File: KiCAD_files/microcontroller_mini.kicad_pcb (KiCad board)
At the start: 4 copper layers, 21 x 51 mm, 38 parts, among them J1 Conn_02x20_Top_Bottom, J2 USB_B_Micro, J8 Conn_02x07_Odd_Even, SW1 SW_Push, U1 STM32G474RE, U2 AT25xxx, U3 WE-TVS-82400102, U4 AP1117-33, Y1 ECS-240-10-33-AGM-TR - 24MHz

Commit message: [Feeder] WIP on the V2 redesign
Former-commit-id: 5bce92fb9a428cd005e74b891f189b6460f88472
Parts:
- R1: value 1 -> 1R

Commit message: WIP : 99 percents of the nets are now routed properly
Former-commit-id: fcbb95e3f0a6512a63faba729c3990d7109d7768
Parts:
- moved J2 0.81 mm to (95.6, 51.2)
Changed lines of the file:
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@@
   )
   (footprint "Connector_USB:USB_Micro-B_Molex_47346-0001" (layer "F.Cu")
-    (at 95.560978 52.01 180)
+    (at 95.560978 51.2 180)
     (descr "Micro USB B receptable with flange, bottom-mount, SMD, right-angle (http://www.molex.com/pdm_docs/sd/473460001_sd.pdf)")
     (tags "Micro B USB SMD")

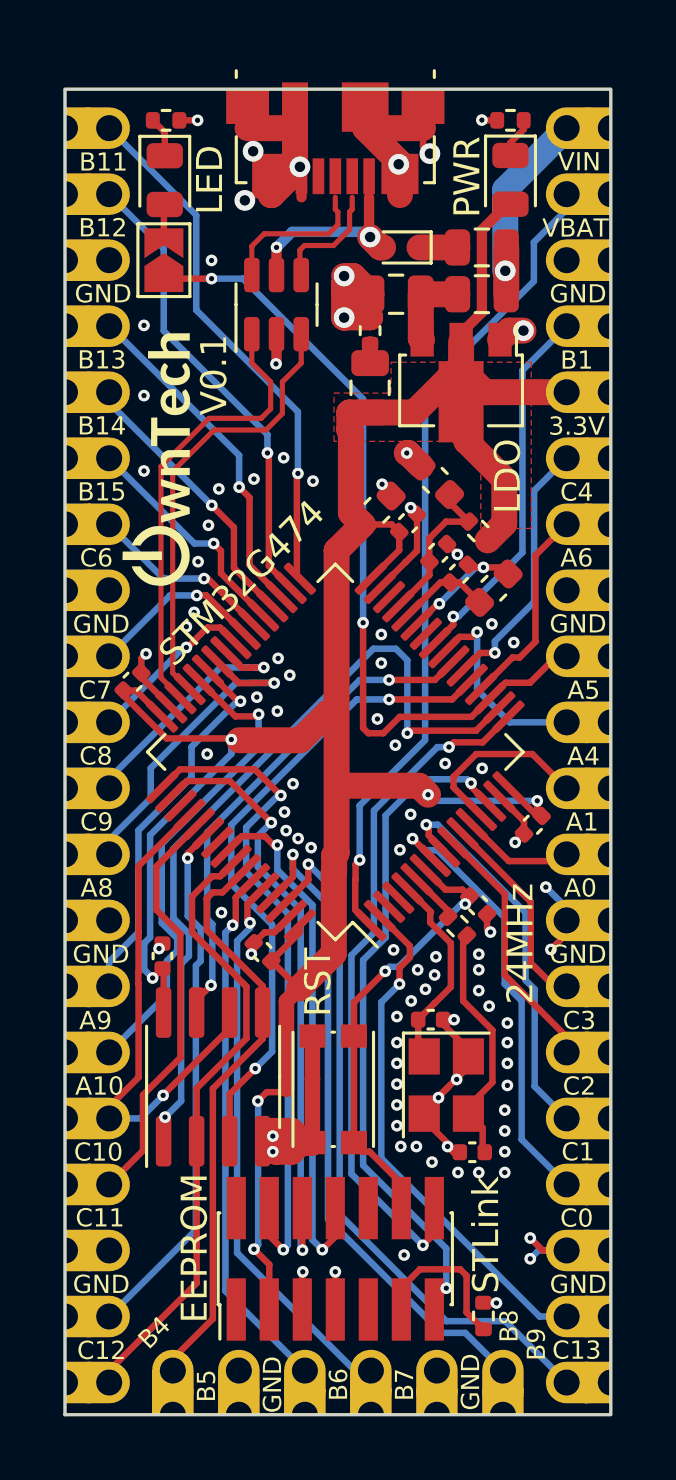
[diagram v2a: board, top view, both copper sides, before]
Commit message: WIP : Started correcting MCU board mistakes
Former-commit-id: 0e34b6d72e10d1eac13c8cf31fc8e8f14d7f468b
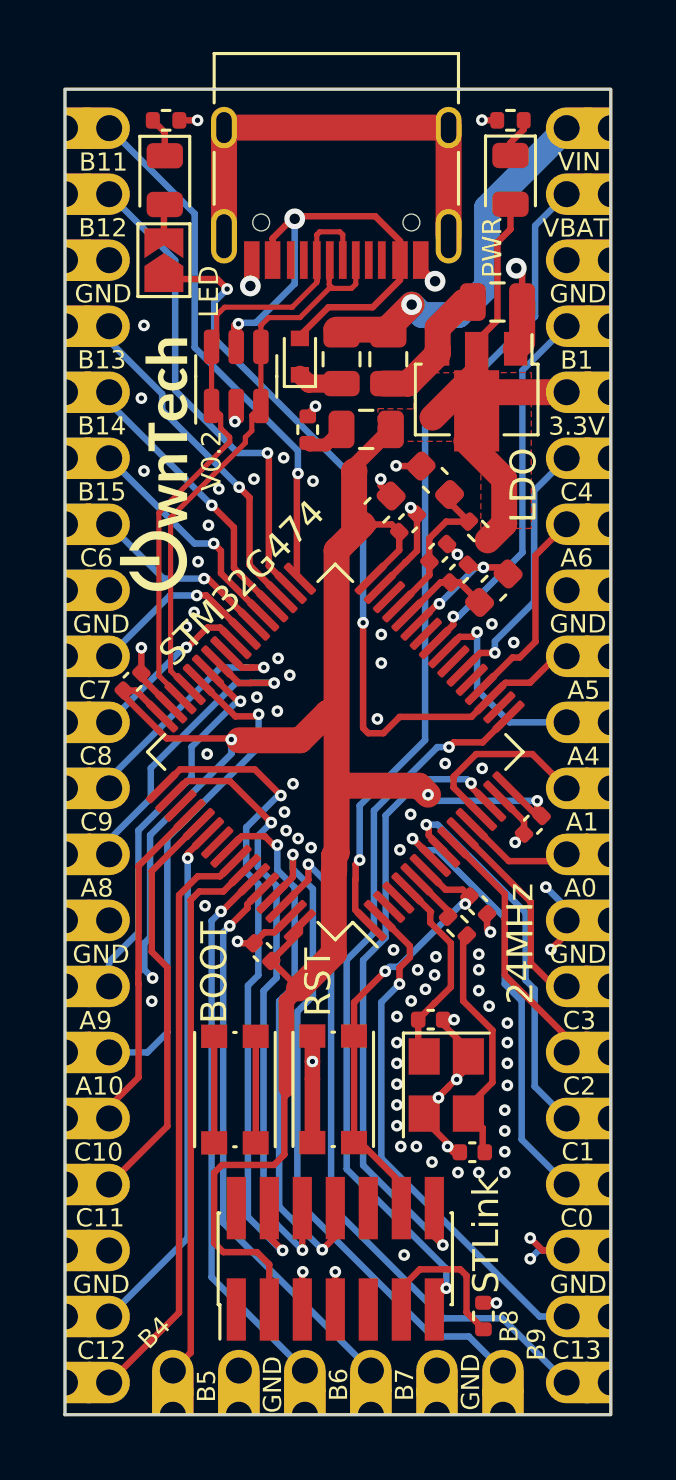
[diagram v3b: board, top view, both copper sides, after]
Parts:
- removed C1: 100nF, Capacitor_SMD:C_0402_1005Metric
- removed U2: AT25xxx, Footprints:SOIC-8_3.9x4.9mm_P1.27mm
- added SW2: KMR241NGLFS, Button_Switch_SMD:SW_Push_1P1T_NO_CK_KMR2, F.Cu at (91.7, 87.8)
- F1, F2: value Fuse_Small -> 350mA
- FB1: value 100Ohm @ 100MHz -> 1000Ohm @ 100MHz
- J2: value USB_B_Micro -> USB_C_Receptacle_USB2.0; footprint Connector_USB:USB_Micro-B_Molex_47346-0001 -> Connector_USB:USB_C_Receptacle_HRO_TYPE-C-31-M-12
- J8: value Conn_02x07_Odd_Even -> FTSH-107-01-F-DV-K
- SW1: value SW_Push -> KMR241NGLFS
- moved F2 6.90 mm to (95.8, 59.7), turned to -90 degrees
- moved D1 5.73 mm to (94.2, 59.6), turned to 90 degrees
- moved R1 4.50 mm to (94.5, 62.4)
- moved F1 4.38 mm to (97.6, 59.7), turned to 90 degrees
- moved C40 3.91 mm to (101.8, 57.5), turned to 0 degrees
- moved U3 3.17 mm to (91.8, 60.4)
- moved C39 1.61 mm to (96.8, 62.4), turned to 180 degrees
- moved U4 0.69 mm to (101.0, 61.0)
- moved J2 0.64 mm to (95.6, 51.8)
- moved G*** 0.22 mm to (88.6, 63.8)
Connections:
- J8 pad 13: /STLINK_RX -> /STLINK_TX
- J8 pad 14: /STLINK_TX -> /STLINK_RX
- U1 pad 21: /EEPROM_WP -> PA7
- U1 pad 55: unconnected-(U1-Pad55) -> (no net)
- U3 pad 4: USB_in_D- -> USB_D-
- U3 pad 6: USB_in_D+ -> USB_D+
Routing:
- net PA4: track 31.0 -> 0.00 mm, vias 2 -> 0
- net /EEPROM_WP: track 25.1 -> 0.00 mm, vias 2 -> 0
- net GNDD: track 95.5 -> 73.0 mm, vias 98 -> 91
- net PC5: track 19.5 -> 0.00 mm, vias 2 -> 0
- net Earth_Protective: track 0.00 -> 17.0 mm
- net VBUS: track 7.21 -> 19.0 mm
- net USB_D+: track 17.5 -> 25.6 mm
- net +3V3: track 103.1 -> 96.3 mm, vias 6 -> 4
- net PC10: track 19.7 -> 13.0 mm, vias 1 -> 0
- net +5VD: track 8.27 -> 14.2 mm
- net USB_in_D+: track 5.86 -> 0.00 mm
- net USB_D-: track 17.2 -> 22.2 mm
- net USB_in_D-: track 4.50 -> 0.00 mm
- net unconnected-(SW2-Pad2): track 0.00 -> 4.10 mm
- net unconnected-(SW2-Pad1): track 0.00 -> 4.10 mm
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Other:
- board text added: "V0.2"
- board text removed: "V0.1"

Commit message: WIP: added features for the RJ45 communication link. Added fast RS485 Added HRTIM Sync Added current share analog bus Added external VREF Added dedicated supply power supply pins for the data manager
Former-commit-id: 7d7dbd6688aaf47caa2ea5f91bf9cef552f6a24c
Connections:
- J8 pad 13: /STLINK_TX -> /STLINK_RX
- J8 pad 14: /STLINK_RX -> /STLINK_TX
- U1 pad 14: /STLINK_RX -> /STLINK_TX
- U1 pad 17: /STLINK_TX -> /STLINK_RX
- U1 pad 18: PA4 -> unconnected-(U1-Pad18)
- U1 pad 21: PA7 -> unconnected-(U1-Pad21)
- U1 pad 23: PC5 -> unconnected-(U1-Pad23)
- U1 pad 3: PC14 -> unconnected-(U1-Pad3)
- U1 pad 30: PB10 -> unconnected-(U1-Pad30)
- U1 pad 4: PC15 -> unconnected-(U1-Pad4)
- U1 pad 51: PA15 -> unconnected-(U1-Pad51)
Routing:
- net /STLINK_TX: track 28.1 -> 24.8 mm
- net /STLINK_RX: track 24.8 -> 28.1 mm
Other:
- board text added: "COMP1OUT"
- board text added: "COMP2OUT"
- board text added: "COMP3OUT"
- board text added: "COMP4+"
- board text added: "COMP4OUT"
- board text added: "COMP5+"
- board text added: "COMP5OUT"
- board text added: "COMP6OUT"
- board text added: "COMP7+"
- board text added: "COMP7OUT"
- board text added: "DAC1OUT"
- board text added: "DAC2OUT"
- board text added: "OPAMP3OUT_DAC3CH2"
- board text added: "OPAMP4OUT_DAC4CH1"
- board text added: "OPAMP5OUT_DAC4CH2"
- board text added: "OPAMP6OUT_DAC3CH1"
- board text removed: "CAN2"

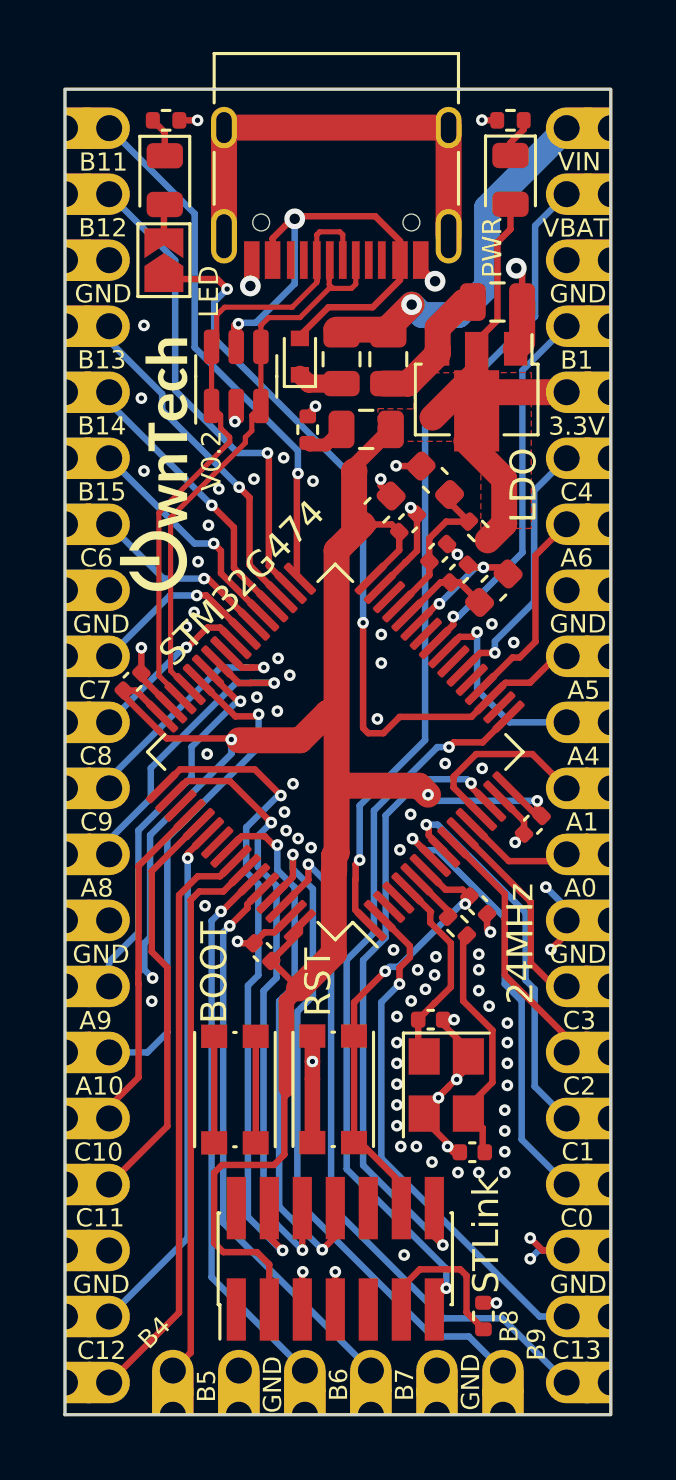
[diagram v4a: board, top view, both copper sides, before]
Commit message: WIP : Finalized the rework of the MCU board. Added extra pins to be able to interact with all the native pinout of the G474 Choosen to deploy the bootloader pin on PC14, it will require a custom bootloader.
Former-commit-id: c1ded6b4e2272d08c1bdd5e172bcf8412ac79a26
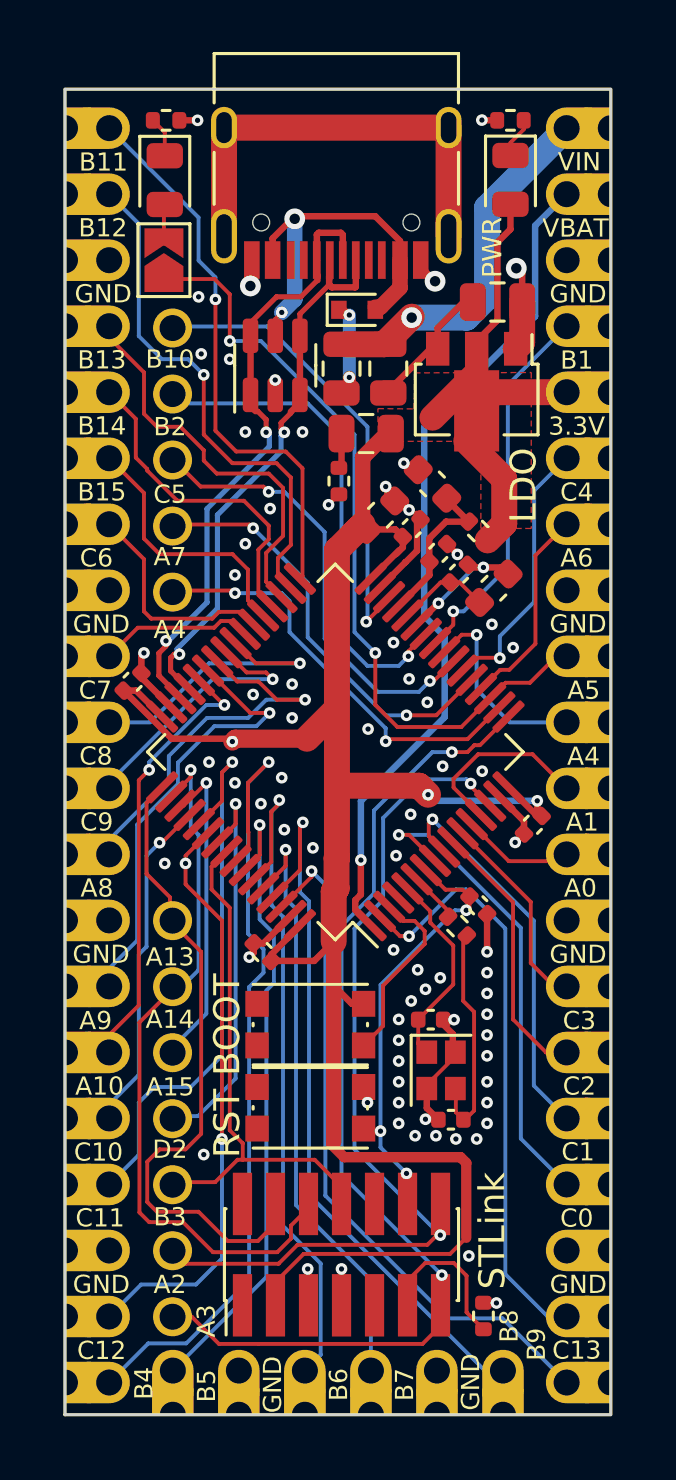
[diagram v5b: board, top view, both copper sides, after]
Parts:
- removed the G*** at (88.6, 63.8)
- added J101: Conn_01x05_Male, Footprints:PinHeader_1x05_P2.54mm_Vertical, F.Cu at (89.3, 68.7)
- added J102: Conn_01x06_Male, Footprints:PinHeader_1x07_P2.54mm_Vertical, F.Cu at (89.3, 81.3)
- Y1: value ECS-240-10-33-AGM-TR - 24MHz -> ECS-240-8-37-CKM-TR3 - 24MHz; footprint Crystal:Crystal_SMD_3225-4Pin_3.2x2.5mm -> Crystal:Crystal_SMD_2016-4Pin_2.0x1.6mm
- moved SW2 3.83 mm to (94.6, 85.3), turned to 180 degrees
- moved D1 2.84 mm to (96.4, 57.8), turned to 0 degrees
- moved R1 2.32 mm to (95.7, 64.4), turned to 90 degrees
- moved U3 1.56 mm to (93.2, 59.9)
- moved C4 1.50 mm to (100.0, 89.0)
- moved SW1 1.13 mm to (94.6, 88.5), turned to 0 degrees
- moved Y1 0.60 mm to (99.6, 87.1)
- moved F1 0.36 mm to (97.6, 60.1)
- moved F2 0.36 mm to (95.8, 60.1)
- moved J8 0.29 mm to (95.8, 94.2)
- moved C10 0.24 mm to (98.5, 66.2)
- moved C6 0.24 mm to (97.3, 65.7)
- moved C12 0.18 mm to (99.3, 64.5)
- moved C39 0.16 mm to (96.8, 62.6)
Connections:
- net /STLINK_RX renamed PA3
- net /STLINK_TX renamed PA2
- net /SWCLK renamed PA14
- net /SWDIO renamed PA13
- net /SWO renamed PB3
- SW2 pad 1: unconnected-(SW2-Pad1) -> PC14
- SW2 pad 2: unconnected-(SW2-Pad2) -> +3V3
- U1 pad 18: unconnected-(U1-Pad18) -> PA4
- U1 pad 21: unconnected-(U1-Pad21) -> PA7
- U1 pad 23: unconnected-(U1-Pad23) -> PC5
- U1 pad 26: unconnected-(U1-Pad26) -> PB2
- U1 pad 3: unconnected-(U1-Pad3) -> PC14
- U1 pad 30: unconnected-(U1-Pad30) -> PB10
- U1 pad 51: unconnected-(U1-Pad51) -> PA15
- U1 pad 55: (no net) -> PD2
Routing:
- net GNDD: track 73.0 -> 37.1 mm, vias 91 -> 76
- net PB2: track 0.00 -> 19.3 mm, vias 0 -> 1
- net PB10: track 0.00 -> 17.9 mm, vias 0 -> 1
- net PC5: track 0.00 -> 17.4 mm, vias 0 -> 2
- net PA4: track 0.00 -> 16.5 mm, vias 0 -> 2
- net PA7: track 0.00 -> 16.3 mm, vias 0 -> 2
- net PD2: track 0.00 -> 15.5 mm, vias 0 -> 1
- net PA15: track 0.00 -> 12.2 mm, vias 0 -> 1
- net PA3: track 28.1 -> 39.8 mm
- net PA2: track 24.8 -> 35.2 mm
- net PB4: track 22.6 -> 32.1 mm, vias 0 -> 1
- net PC14: track 0.00 -> 7.13 mm
- net PC11: track 15.8 -> 22.0 mm, vias 0 -> 1
- net PB6: track 21.1 -> 26.6 mm
- net VBUS: track 19.0 -> 14.4 mm
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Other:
- board text added: "A13"
- board text added: "A14"
- board text added: "A15"
- board text added: "A2"
- board text added: "A3"
- board text added: "A7"
- board text added: "B10"
- board text added: "B2"
- board text added: "B3"
- board text added: "C5"
- board text added: "D2"
- board text removed: "V0.2"

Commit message: WIP : Refined the crystal GND keepout, polished the bottom overlay
Former-commit-id: 2906c1a23d44a8ddcb814e6c8993671dfbd082db
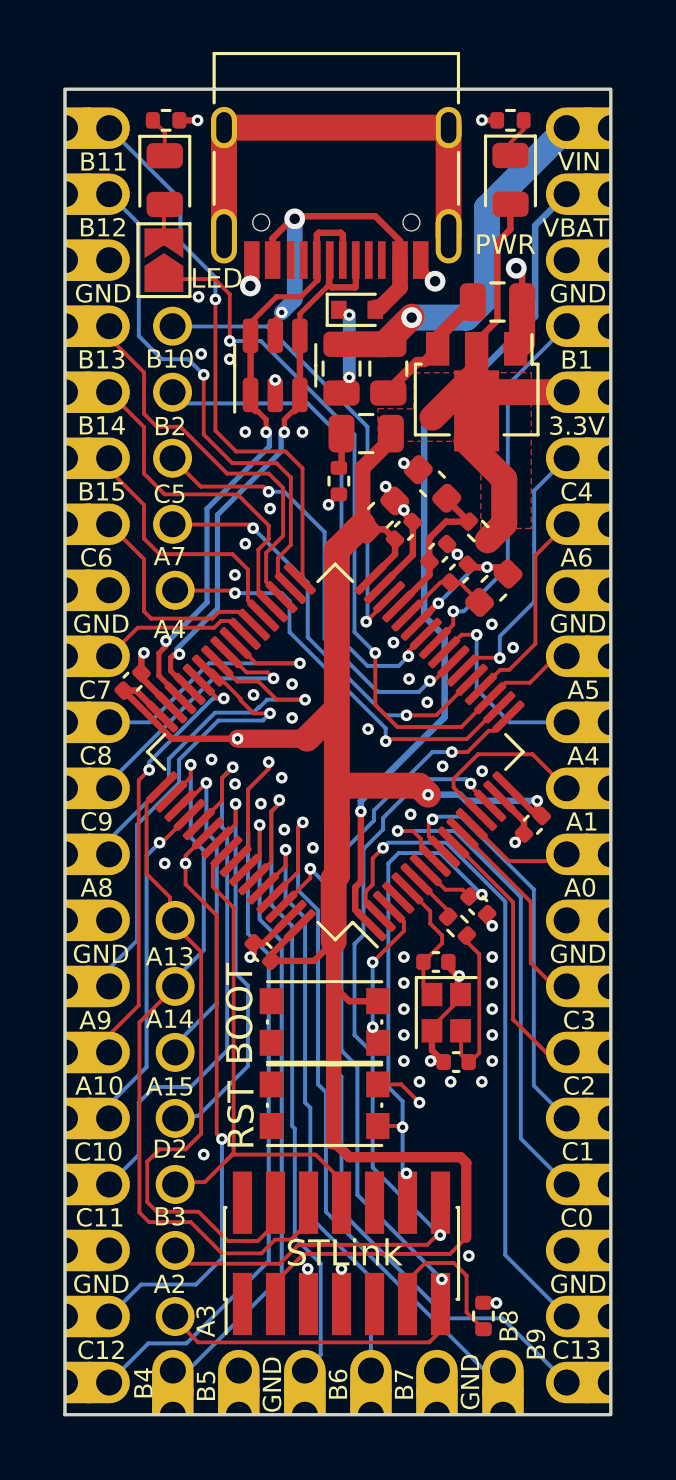
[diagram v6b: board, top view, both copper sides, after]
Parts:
- moved G*** 41.5 mm to (111.5, 32.9)
- moved C3 2.23 mm to (99.4, 82.9)
- moved Y1 2.23 mm to (99.8, 84.8)
- moved C4 2.23 mm to (100.2, 86.7)
- moved SW1 0.56 mm to (95.2, 88.4)
- moved SW2 0.56 mm to (95.2, 85.2)
- moved C10 0.32 mm to (98.2, 66.3)
- moved J102 0.10 mm to (89.4, 81.3)
- moved J101 0.07 mm to (89.3, 68.6)
- moved J8 0.05 mm to (95.8, 94.1)
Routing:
- net GNDD: track 37.1 -> 66.6 mm, vias 76 -> 65
- net /NRST: track 16.9 -> 21.6 mm
- net PC13: track 22.9 -> 25.8 mm
- net /HSE_IN: track 7.72 -> 5.07 mm
- net Net-(C4-Pad1): track 8.88 -> 6.59 mm
- net PC14: track 7.13 -> 6.05 mm, vias 0 -> 2
- net PC0: track 18.6 -> 19.7 mm
- net PC1: track 15.2 -> 16.0 mm
- net PB5: track 24.8 -> 25.4 mm
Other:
- board text added: "LED"
